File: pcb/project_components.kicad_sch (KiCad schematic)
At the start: 10 parts, among them J1 DA15_Receptacle, J2 Controller Input, SW1 09.10201.02, U6 SN74LVC8T245, U7 SN74AVC4T245PW

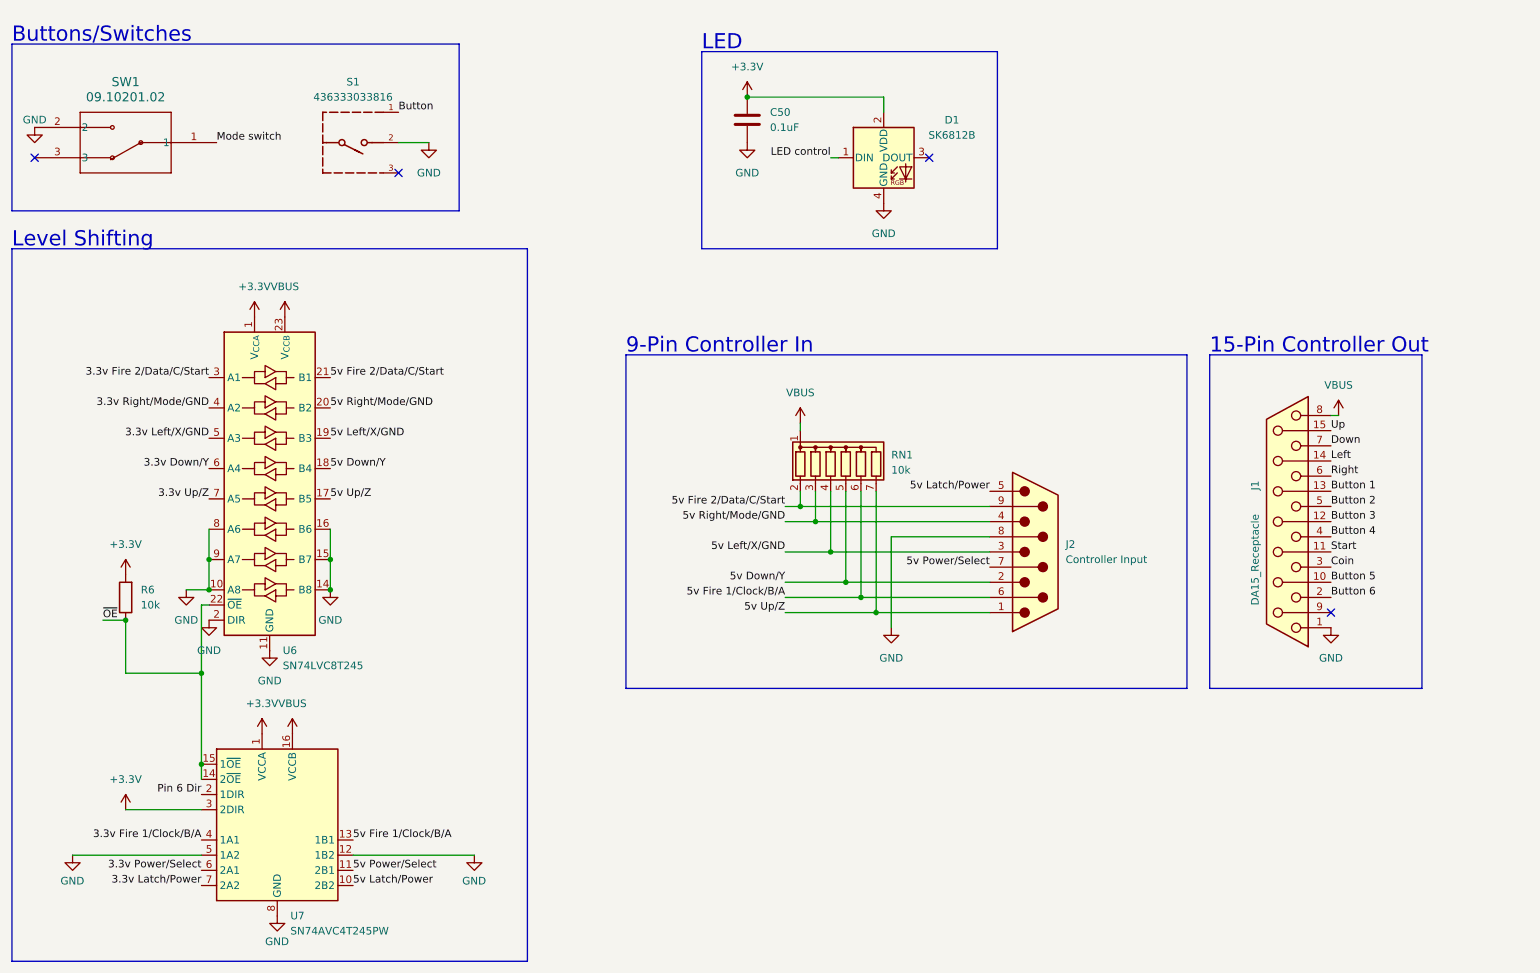
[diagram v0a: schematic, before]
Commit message: Update the schematic to properly use hierarchical sheets, update the PCB to match, tidy up some weirdnesses (button with a "U" refdes, both S and SW refdes, etc)
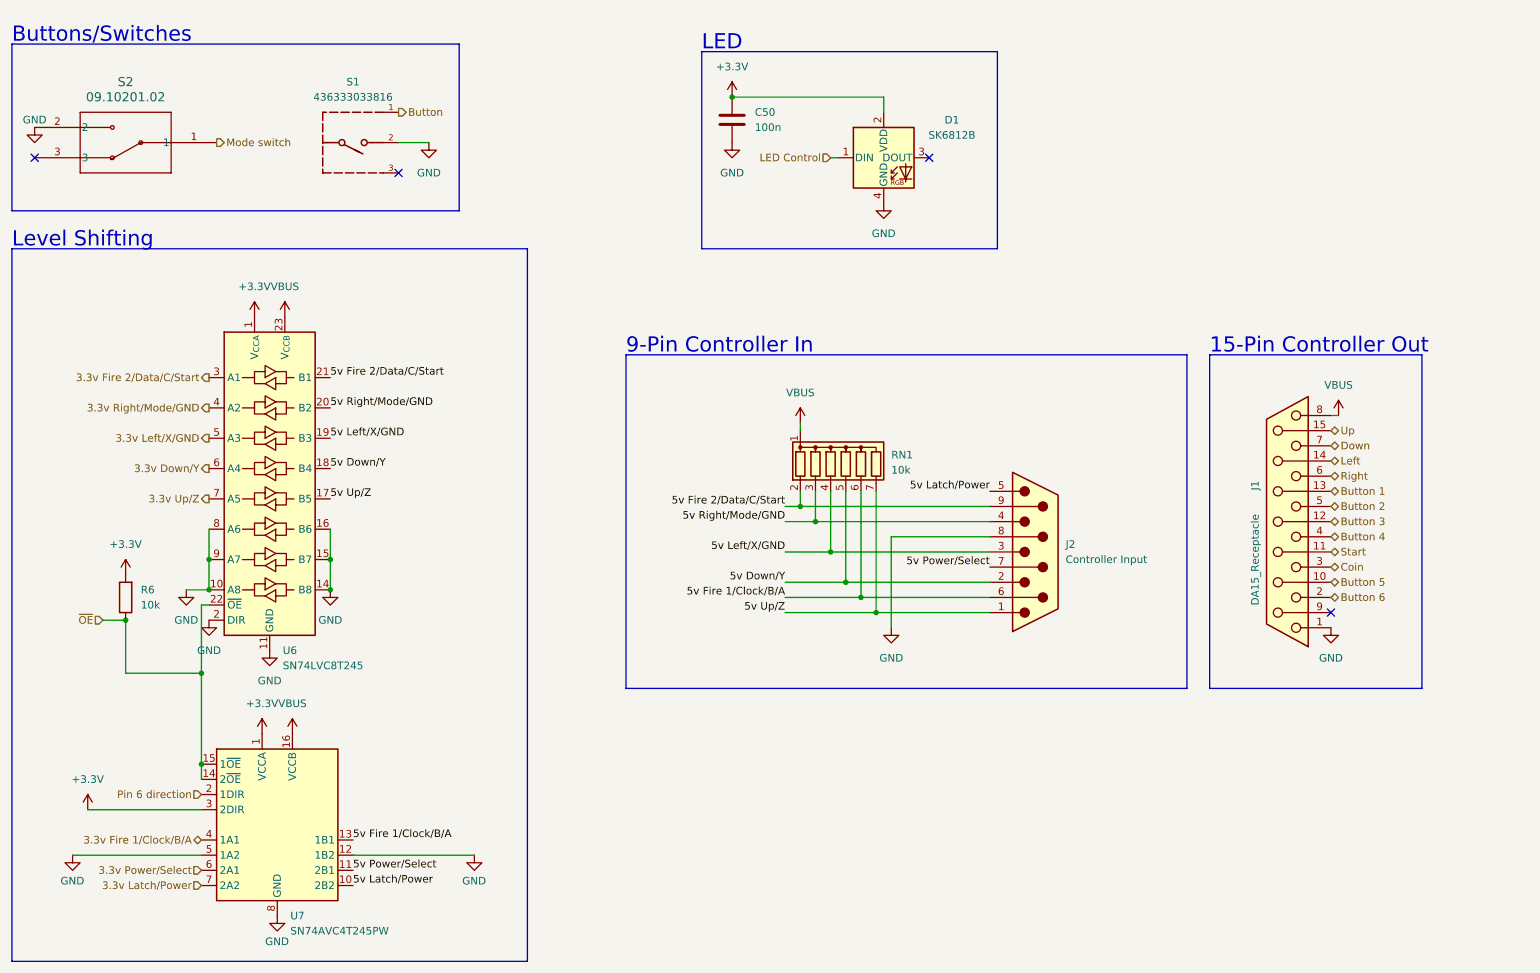
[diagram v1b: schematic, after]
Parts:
- C50: value 0.1uF -> 100n
- renumbered SW1 to S2
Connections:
- net LED control renamed LED Control
- net Pin 6 Dir renamed Pin 6 direction
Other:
- moved on the sheet: C50

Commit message: Update PCB to v1.1:  * Update level shifting to a component that actually supports 5V  * Make both D-Sub connectors the same size in terms of pin offset (added bonus of making the board smaller)  * Update a couple of footprints that have changed name  * Add a switch for USB host/device,
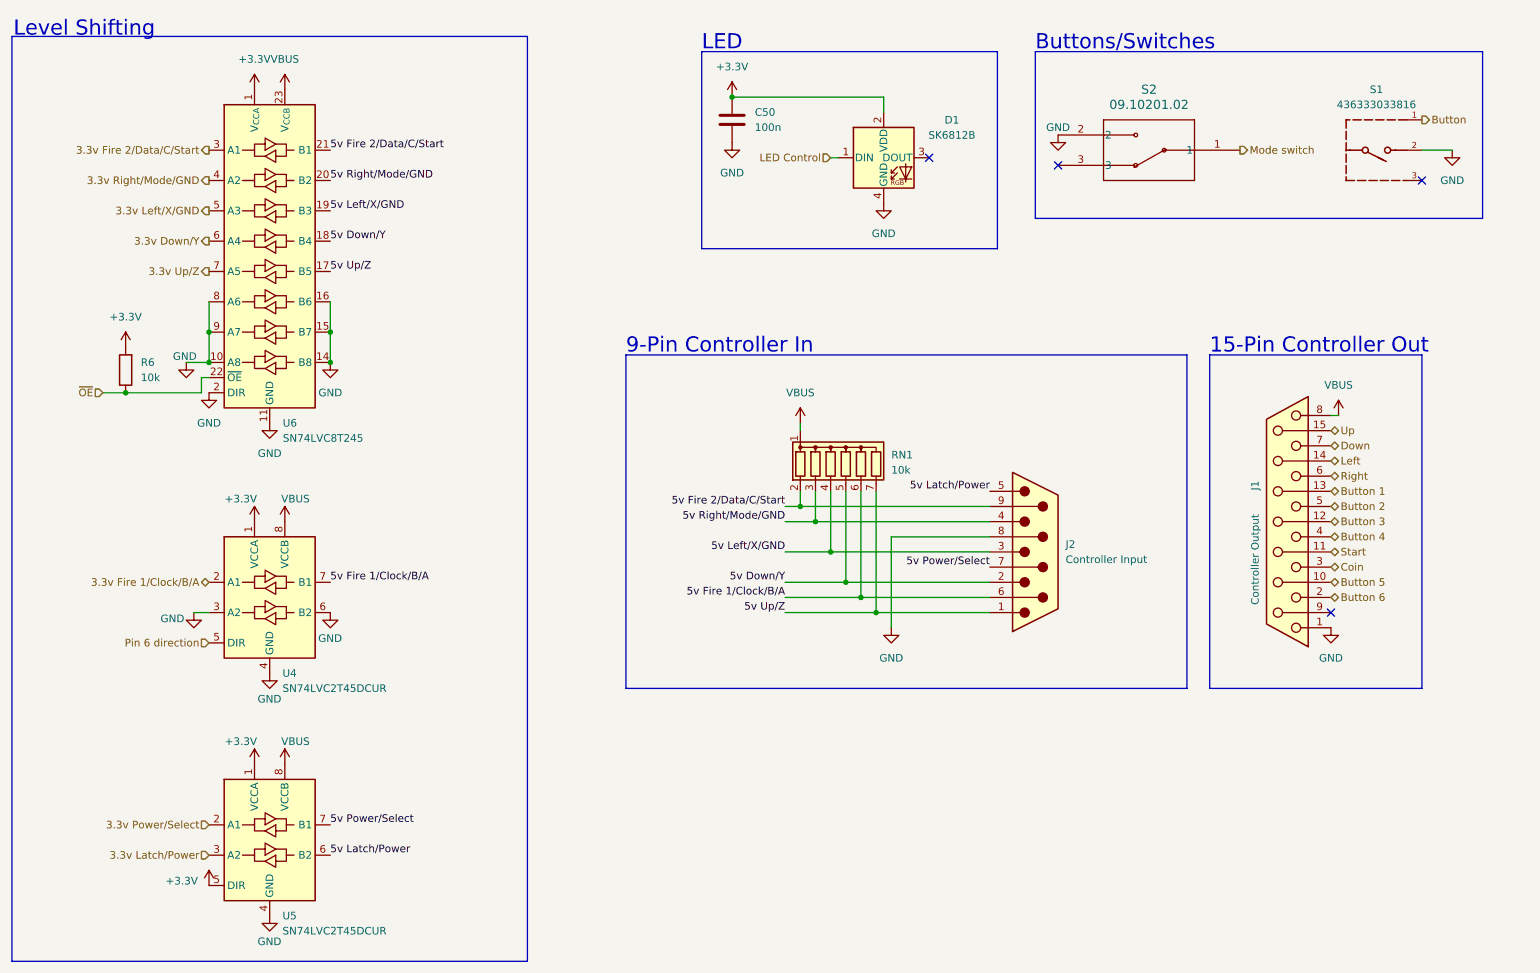
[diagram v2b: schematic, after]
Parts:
- removed U7: SN74AVC4T245PW, Package_SO:TSSOP-16_4.4x5mm_P0.65mm, symbol Logic_LevelTranslator:SN74AVC4T245PW
- added U4, U5: SN74LVC2T45DCUR, Package_SO:VSSOP-8_2.3x2mm_P0.5mm, symbol Logic_LevelTranslator:SN74LVC2T45DCUR
- J1: value DA15_Receptacle -> Controller Output; footprint Connector_Dsub:DSUB-15_Female_Horizontal_P2.77x2.84mm_EdgePinOffset9.90mm_Housed_MountingHolesOffset11.32mm -> Connector_Dsub:DSUB-15_Socket_Horizontal_P2.77x2.84mm_EdgePinOffset7.70mm_Housed_MountingHolesOffset9.12mm
- J2: footprint Connector_Dsub:DSUB-9_Male_Horizontal_P2.77x2.84mm_EdgePinOffset7.70mm_Housed_MountingHolesOffset9.12mm -> Connector_Dsub:DSUB-9_Pins_Horizontal_P2.77x2.84mm_EdgePinOffset7.70mm_Housed_MountingHolesOffset9.12mm
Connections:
- net +3.3V: now also U4.1 (VCCA), U5.1 (VCCA), U5.5 (DIR)
- net 3.3v Fire 1/Clock/B/A: now also U4.2 (A1)
- net 3.3v Latch/Power: now also U5.3 (A2)
- net 3.3v Power/Select: now also U5.2 (A1)
- net 5v Fire 1/Clock/B/A: now also U4.7 (B1)
- net 5v Latch/Power: now also U5.6 (B2)
- net 5v Power/Select: now also U5.7 (B1)
- net GND: now also U4.3 (A2), U4.4 (GND), U4.6 (B2), U5.4 (GND)
- net Pin 6 direction: now also U4.5 (DIR)
- net VBUS: now also U4.8 (VCCB), U5.8 (VCCB)
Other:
- moved on the sheet: R6, S1, S2, U6
